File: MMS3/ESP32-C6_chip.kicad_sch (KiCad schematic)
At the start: 44 parts, among them J5 Conn_Coaxial, SW3 TC-6615Z-12.5-260, U11 ESP32-C6_C5364646, U8 ZD25Q128CSIGT, X2 40MHz, 15pF

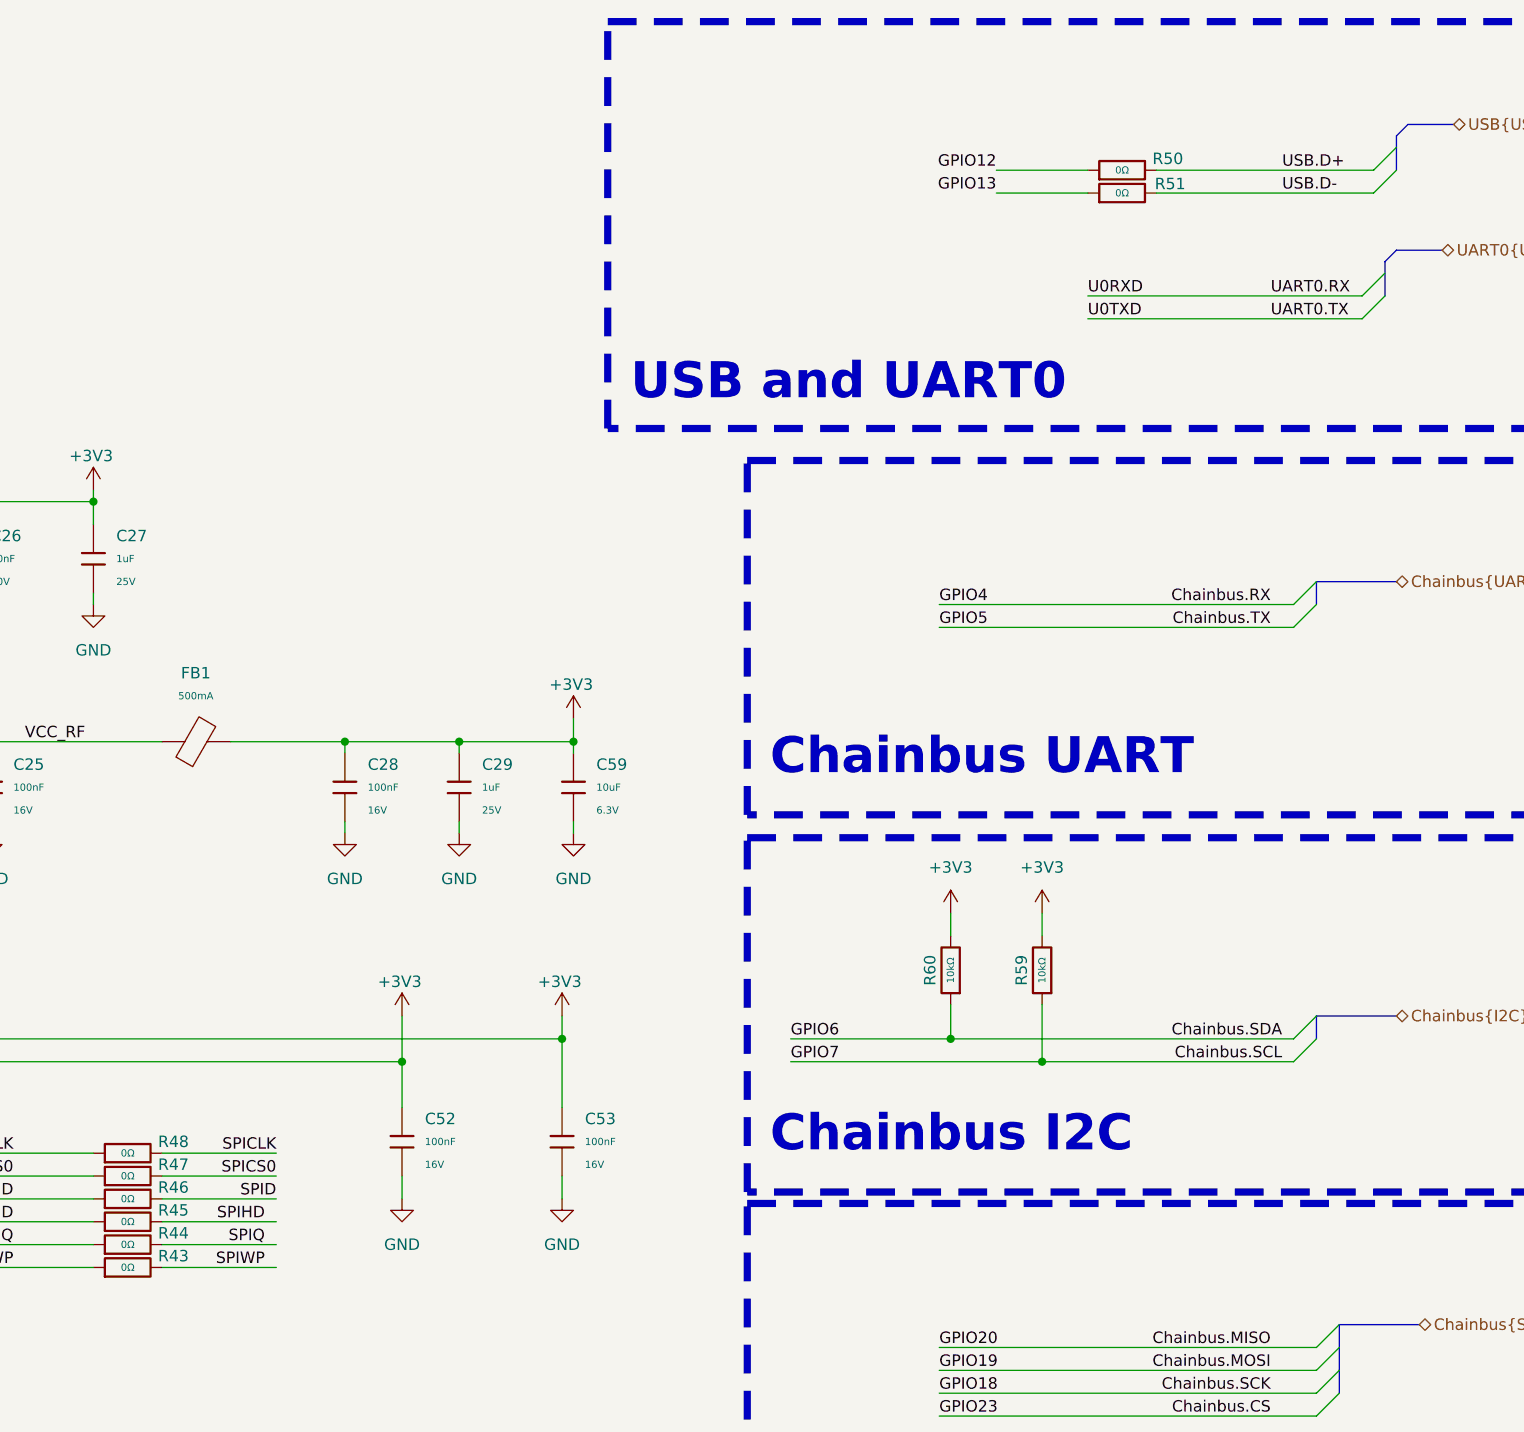
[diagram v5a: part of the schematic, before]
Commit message: fixed swapped RX/TX & D+/D_
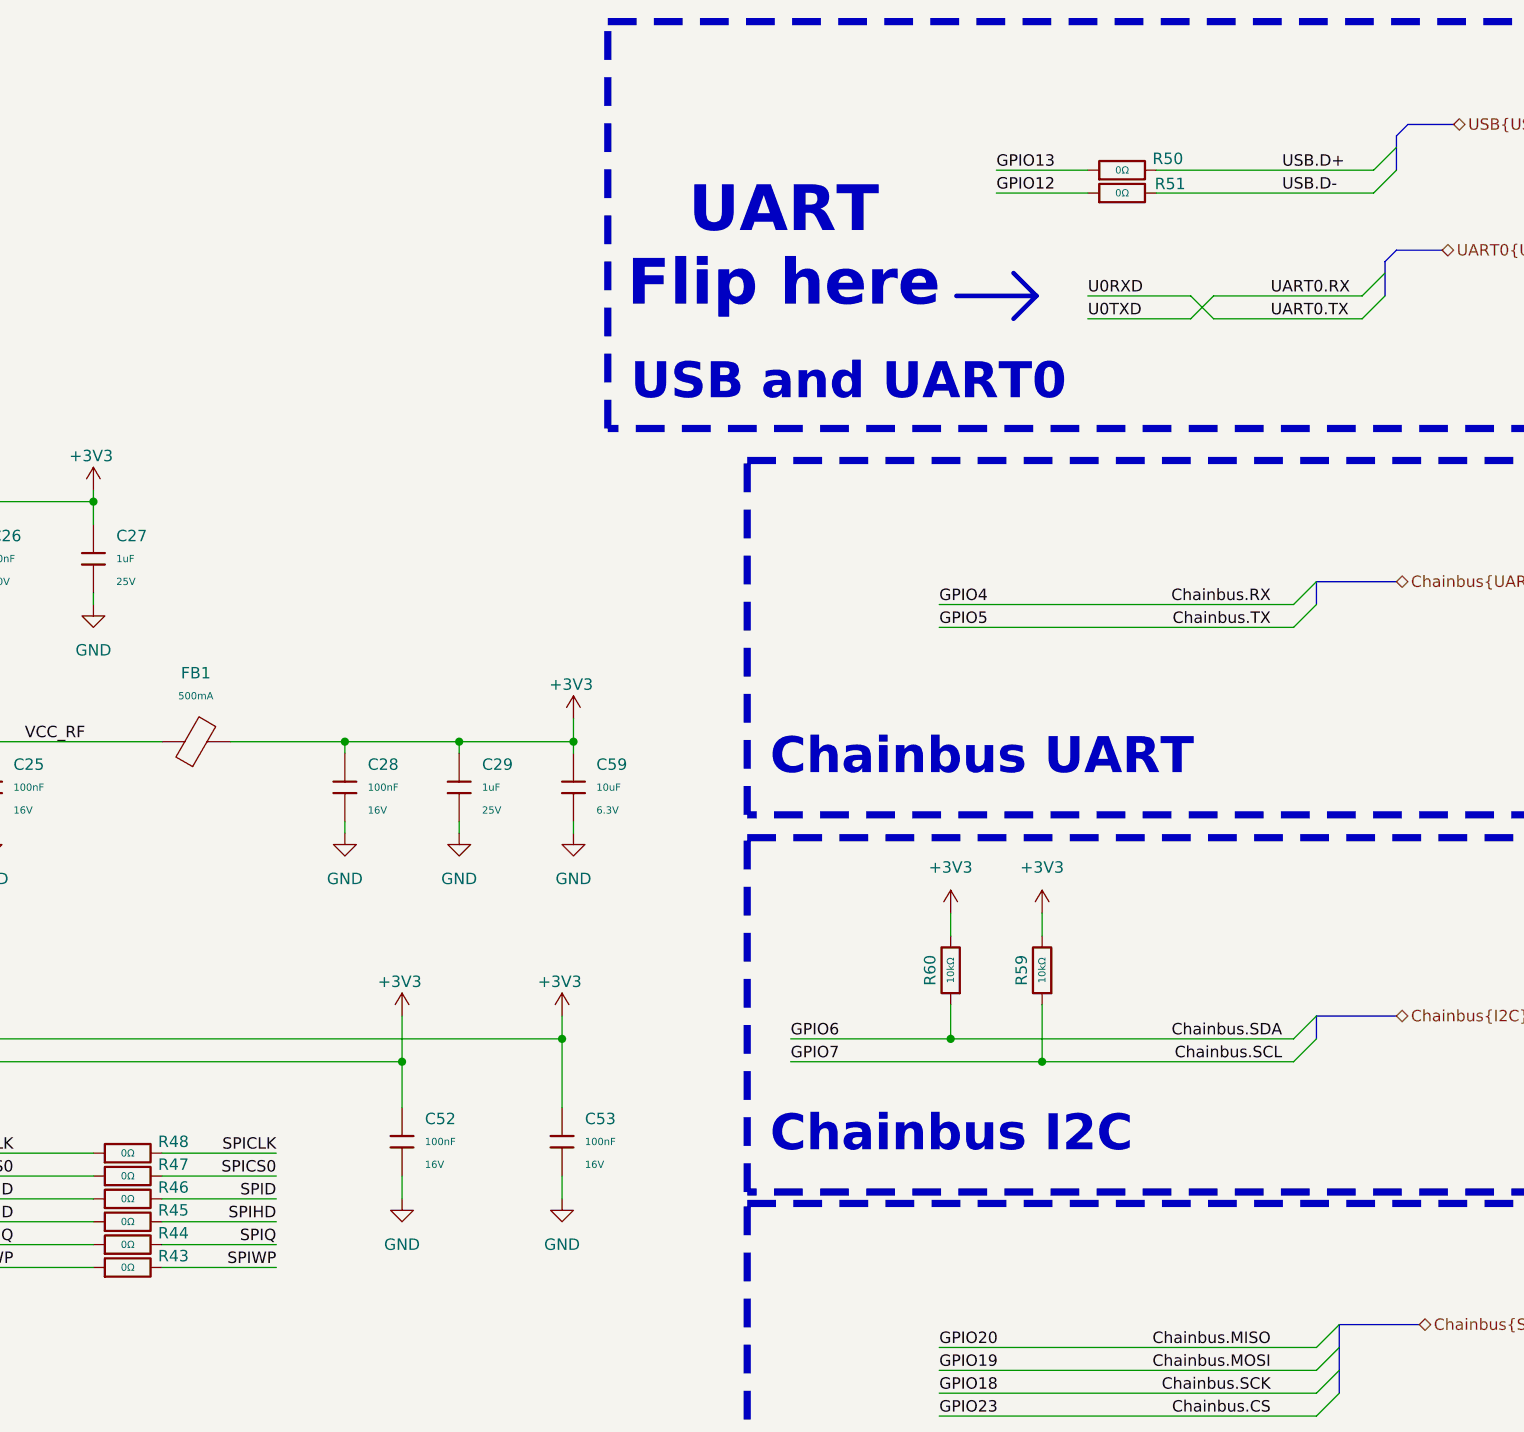
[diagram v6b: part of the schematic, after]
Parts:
- L3: footprint PCM_JLCPCB:C_0402 -> PCM_JLCPCB:L_0402
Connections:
- net GPIO12: now also R51.1; no longer R50.1
- net GPIO13: now also R50.1; no longer R51.1
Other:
- note added: "UART Flip here"
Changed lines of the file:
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@@
 		)
 	)
+	(text "UART\nFlip here"
+		(exclude_from_sim no)
+		(at 316.738 40.386 0)
+		(effects
+			(font
+				(size 5.08 5.08)
+				(thickness 1.016)
+				(bold yes)
+				(color 255 0 0 1)
+			)
+		)
+	)
 	(text "40MHz Oscilator"
 		(exclude_from_sim no)
@@
 		)
 	)
+	(polyline
+		(pts
+			(xy 342.265 48.26) (xy 344.805 45.72)
+		)
+		(stroke
+			(width 0.508)
+			(type default)
+			(color 255 0 0 1)
+		)
+	)
 	(wire
 		(pts
@@
 		)
 	)
+	(wire
+		(pts
+			(xy 361.95 45.72) (xy 364.49 48.26)
+		)
+		(stroke
+			(width 0)
+			(type default)
+		)
+	)
 	(bus
 		(pts
@@
 	(wire
 		(pts
+			(xy 247.65 151.13) (xy 260.35 151.13)
+		)
+		(stroke
+			(width 0)
+			(type default)
+		)
+	)
+	(wire
+		(pts
 			(xy 226.06 68.58) (xy 226.06 71.12)
 		)
@@
 	(wire
 		(pts
-			(xy 350.52 48.26) (xy 381 48.26)
-		)
-		(stroke
-			(width 0)
-			(type default)
-		)
-	)
-	(wire
-		(pts
 			(xy 148.59 121.92) (xy 176.53 121.92)
 		)
@@
 	(wire
 		(pts
-			(xy 260.35 151.13) (xy 247.65 151.13)
-		)
-		(stroke
-			(width 0)
-			(type default)
-		)
-	)
-	(wire
-		(pts
 			(xy 240.03 71.12) (xy 240.03 68.58)
 		)
@@
 		)
 	)
+	(polyline
+		(pts
+			(xy 335.915 45.72) (xy 344.805 45.72)
+		)
+		(stroke
+			(width 0.508)
+			(type default)
+			(color 255 0 0 1)
+		)
+	)
 	(wire
 		(pts
@@
 	(wire
 		(pts
+			(xy 247.65 153.67) (xy 260.35 153.67)
+		)
+		(stroke
+			(width 0)
+			(type default)
+		)
+	)
+	(wire
+		(pts
 			(xy 330.2 213.36) (xy 370.84 213.36)
 		)
@@
 	(wire
 		(pts
-			(xy 260.35 153.67) (xy 247.65 153.67)
+			(xy 350.52 45.72) (xy 361.95 45.72)
 		)
 		(stroke
@@
 		)
 	)
+	(polyline
+		(pts
+			(xy 344.805 45.72) (xy 342.265 43.18)
+		)
+		(stroke
+			(width 0.508)
+			(type default)
+			(color 255 0 0 1)
+		)
+	)
 	(bus
 		(pts
@@
 	(wire
 		(pts
+			(xy 350.52 48.26) (xy 361.95 48.26)
+		)
+		(stroke
+			(width 0)
+			(type default)
+		)
+	)
+	(wire
+		(pts
 			(xy 59.69 255.27) (xy 59.69 257.81)
 		)
@@
 	(wire
 		(pts
+			(xy 247.65 148.59) (xy 260.35 148.59)
+		)
+		(stroke
+			(width 0)
+			(type default)
+		)
+	)
+	(wire
+		(pts
 			(xy 217.17 123.19) (xy 217.17 125.73)
 		)
@@
 	(wire
 		(pts
+			(xy 364.49 45.72) (xy 381 45.72)
+		)
+		(stroke
+			(width 0)
+			(type default)
+		)
+	)
+	(wire
+		(pts
 			(xy 330.2 210.82) (xy 370.84 210.82)
 		)
@@
 	(wire
 		(pts
+			(xy 364.49 45.72) (xy 361.95 48.26)
+		)
+		(stroke
+			(width 0)
+			(type default)
+		)
+	)
+	(wire
+		(pts
 			(xy 292.1 125.73) (xy 292.1 128.27)
 		)
@@
 	(wire
 		(pts
-			(xy 260.35 148.59) (xy 247.65 148.59)
-		)
-		(stroke
-			(width 0)
-			(type default)
-		)
-	)
-	(wire
-		(pts
 			(xy 280.67 95.25) (xy 280.67 96.52)
 		)
@@
 	(wire
 		(pts
-			(xy 350.52 45.72) (xy 381 45.72)
-		)
-		(stroke
-			(width 0)
-			(type default)
-		)
-	)
-	(wire
-		(pts
 			(xy 54.61 255.27) (xy 54.61 254)
 		)
@@
 	(wire
 		(pts
+			(xy 364.49 48.26) (xy 381 48.26)
+		)
+		(stroke
+			(width 0)
+			(type default)
+		)
+	)
+	(wire
+		(pts
 			(xy 22.86 171.45) (xy 39.37 171.45)
 		)
@@
 	)
 	(label "SPIHD"
-		(at 259.08 148.59 180)
+		(at 260.35 148.59 180)
 		(effects
 			(font
@@
 	)
 	(label "SPIWP"
-		(at 259.08 153.67 180)
+		(at 260.35 153.67 180)
 		(effects
 			(font
@@
 	)
 	(label "SPIQ"
-		(at 259.08 151.13 180)
+		(at 260.35 151.13 180)
 		(effects
 			(font
@@
 	)
 	(label "GPIO13"
-		(at 340.36 34.29 180)
+		(at 340.36 31.75 0)
 		(effects
 			(font
 				(size 1.27 1.27)
 			)
-			(justify right bottom)
+			(justify left bottom)
 		)
 	)
@@
 	)
 	(label "GPIO12"
-		(at 340.36 31.75 180)
+		(at 340.36 34.29 0)
 		(effects
 			(font
 				(size 1.27 1.27)
 			)
-			(justify right bottom)
+			(justify left bottom)
 		)
 	)
@@
 			)
 		)
-		(property "Footprint" "PCM_JLCPCB:C_0402"
+		(property "Footprint" "PCM_JLCPCB:L_0402"
 			(at 52.07 39.37 0)
 			(hide yes)
